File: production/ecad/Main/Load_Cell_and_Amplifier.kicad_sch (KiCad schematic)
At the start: 19 parts, among them Q3 MMBT4403, U3 HX711

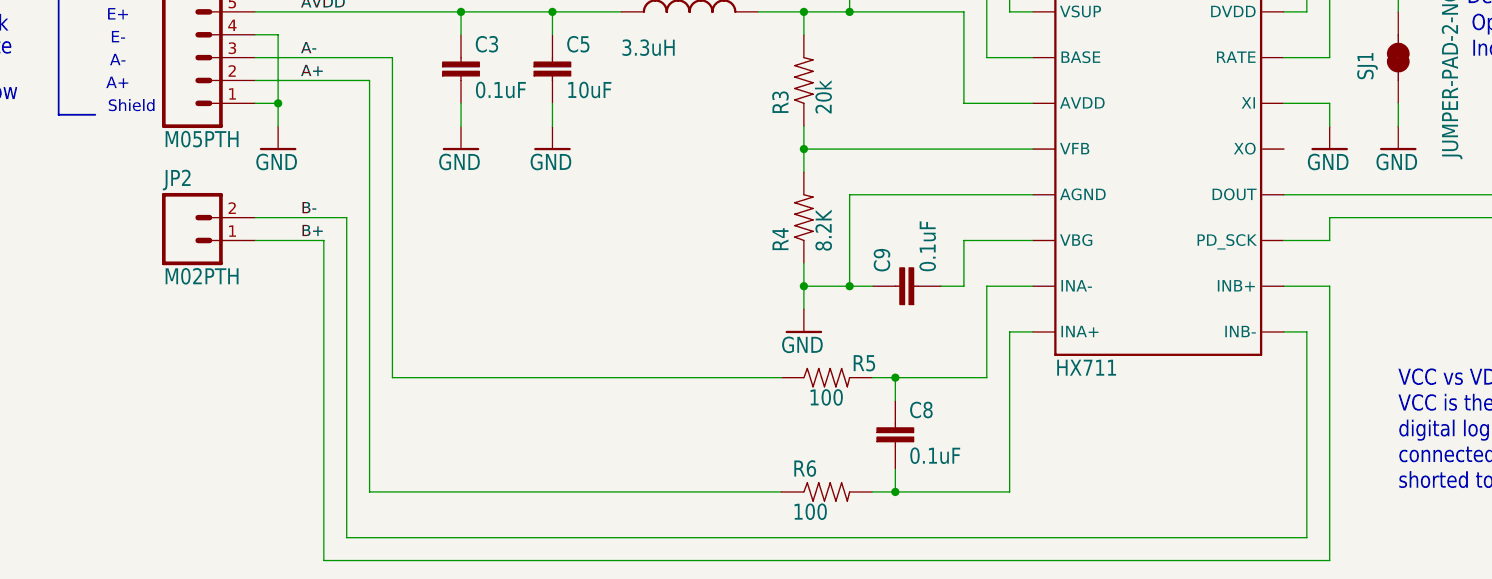
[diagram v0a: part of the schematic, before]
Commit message: deleted B pins bc we won use them
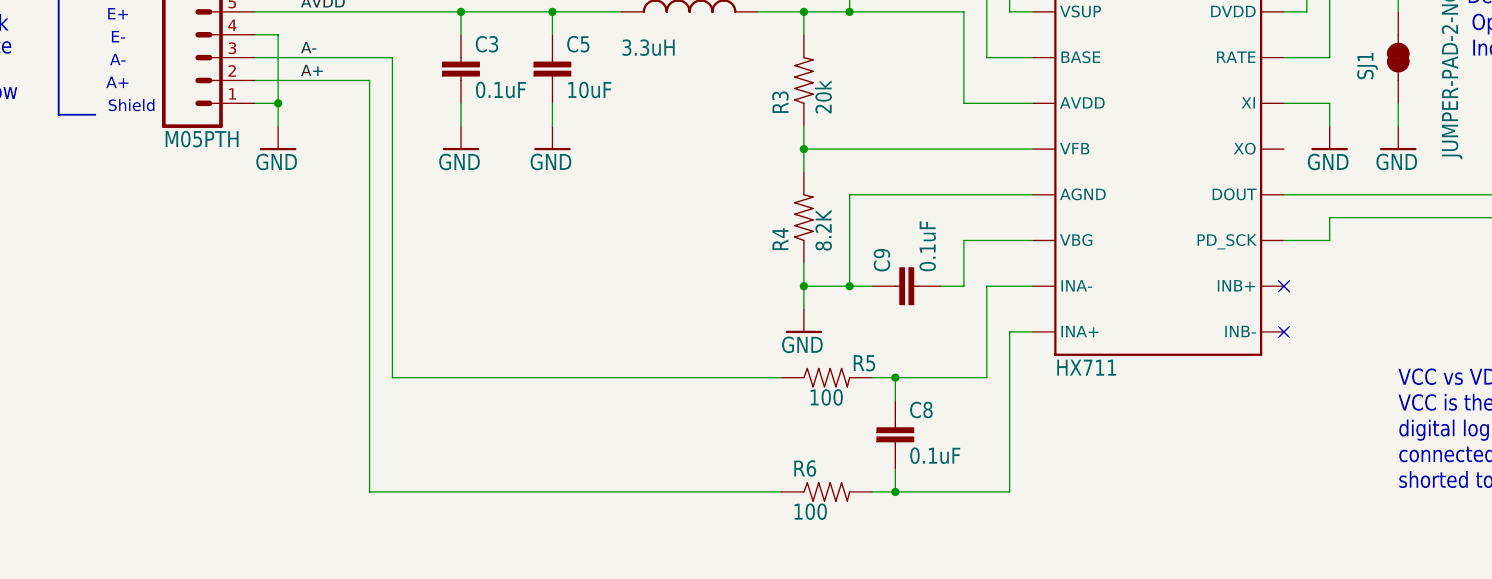
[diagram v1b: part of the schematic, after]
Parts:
- removed JP2: M02PTH, Load Cell and Amplifier:1X02, symbol Load Cell and Amplifier-eagle-import:M02PTH
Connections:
- net B+: no longer names the net of U3.10 (INB+)
- net B-: no longer names the net of U3.9 (INB-)
- no-connect marks 0 -> 2
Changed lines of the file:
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@@
 		(color 0 0 0 0)
 	)
+	(no_connect
+		(at 190.5 106.68)
+	)
+	(no_connect
+		(at 190.5 101.6)
+	)
 	(wire
 		(pts
@@
 	(wire
 		(pts
-			(xy 190.5 106.68) (xy 193.04 106.68)
-		)
-		(stroke
-			(width 0.1524)
-			(type solid)
-		)
-	)
-	(wire
-		(pts
 			(xy 190.5 81.28) (xy 195.58 81.28)
 		)
@@
 	(wire
 		(pts
-			(xy 83.82 96.52) (xy 76.2 96.52)
-		)
-		(stroke
-			(width 0.1524)
-			(type solid)
-		)
-	)
-	(wire
-		(pts
 			(xy 144.78 101.6) (xy 142.24 101.6)
 		)
@@
 	(wire
 		(pts
-			(xy 193.04 106.68) (xy 193.04 129.54)
-		)
-		(stroke
-			(width 0.1524)
-			(type solid)
-		)
-	)
-	(wire
-		(pts
 			(xy 101.6 55.88) (xy 101.6 53.34)
 		)
@@
 		(pts
 			(xy 203.2 68.58) (xy 203.2 71.12)
-		)
-		(stroke
-			(width 0.1524)
-			(type solid)
-		)
-	)
-	(wire
-		(pts
-			(xy 83.82 132.08) (xy 83.82 96.52)
 		)
 		(stroke
@@
 	(wire
 		(pts
-			(xy 86.36 129.54) (xy 86.36 93.98)
-		)
-		(stroke
-			(width 0.1524)
-			(type solid)
-		)
-	)
-	(wire
-		(pts
 			(xy 129.54 45.72) (xy 129.54 43.18)
-		)
-		(stroke
-			(width 0.1524)
-			(type solid)
-		)
-	)
-	(wire
-		(pts
-			(xy 86.36 93.98) (xy 76.2 93.98)
 		)
 		(stroke
@@
 	(wire
 		(pts
-			(xy 195.58 132.08) (xy 83.82 132.08)
-		)
-		(stroke
-			(width 0.1524)
-			(type solid)
-		)
-	)
-	(wire
-		(pts
 			(xy 137.16 104.14) (xy 137.16 101.6)
 		)
@@
 		(pts
 			(xy 220.98 96.52) (xy 220.98 99.06)
-		)
-		(stroke
-			(width 0.1524)
-			(type solid)
-		)
-	)
-	(wire
-		(pts
-			(xy 190.5 101.6) (xy 195.58 101.6)
 		)
 		(stroke
@@
 	(wire
 		(pts
-			(xy 193.04 129.54) (xy 86.36 129.54)
-		)
-		(stroke
-			(width 0.1524)
-			(type solid)
-		)
-	)
-	(wire
-		(pts
 			(xy 223.52 96.52) (xy 220.98 96.52)
 		)
@@
 		(pts
 			(xy 203.2 81.28) (xy 203.2 83.82)
-		)
-		(stroke
-			(width 0.1524)
-			(type solid)
-		)
-	)
-	(wire
-		(pts
-			(xy 195.58 101.6) (xy 195.58 132.08)
 		)
 		(stroke
@@
 	(label "AVDD"
 		(at 81.28 71.12 0)
-		(fields_autoplaced yes)
-		(effects
-			(font
-				(size 1.2446 1.2446)
-			)
-			(justify left bottom)
-		)
-	)
-	(label "B+"
-		(at 81.28 96.52 0)
-		(fields_autoplaced yes)
-		(effects
-			(font
-				(size 1.2446 1.2446)
-			)
-			(justify left bottom)
-		)
-	)
-	(label "B-"
-		(at 81.28 93.98 0)
 		(fields_autoplaced yes)
 		(effects
@@
 					(unit 1)
 				)
-			)
-		)
-	)
-	(symbol
-		(lib_id "Load Cell and Amplifier-eagle-import:M02PTH")
-		(at 68.58 96.52 0)
-		(unit 1)
-		(exclude_from_sim no)
-		(in_bom yes)
-		(on_board yes)
-		(dnp no)
-		(property "Reference" "JP2"
-			(at 66.04 90.678 0)
-			(effects
-				(font
-					(size 1.778 1.5113)
-				)
-				(justify left bottom)
-			)
-		)
-		(property "Value" "M02PTH"
-			(at 66.04 101.6 0)
-			(effects
-				(font
-					(size 1.778 1.5113)
-				)
-				(justify left bottom)
-			)
-		)
-		(property "Footprint" "Load Cell and Amplifier:1X02"
-			(at 68.58 96.52 0)
-			(effects
-				(font
-					(size 1.27 1.27)
-				)
-				(hide yes)
-			)
-		)
-		(property "Datasheet" ""
-			(at 68.58 96.52 0)
-			(effects
-				(font
-					(size 1.27 1.27)
-				)
-				(hide yes)
-			)
-		)
-		(property "Description" ""
-			(at 68.58 96.52 0)
-			(effects
-				(font
-					(size 1.27 1.27)
-				)
-				(hide yes)
-			)
-		)
-		(pin "1"
-		)
-		(pin "2"
-		)
-		(instances
-			(project "Main"
-				(path "/a34d77bc-8f6a-417e-a206-3165e6c5c658/1fa8e4ec-3b8f-41b7-8956-25ba2b294586"
-					(reference "JP2")
-					(unit 1)
-				)

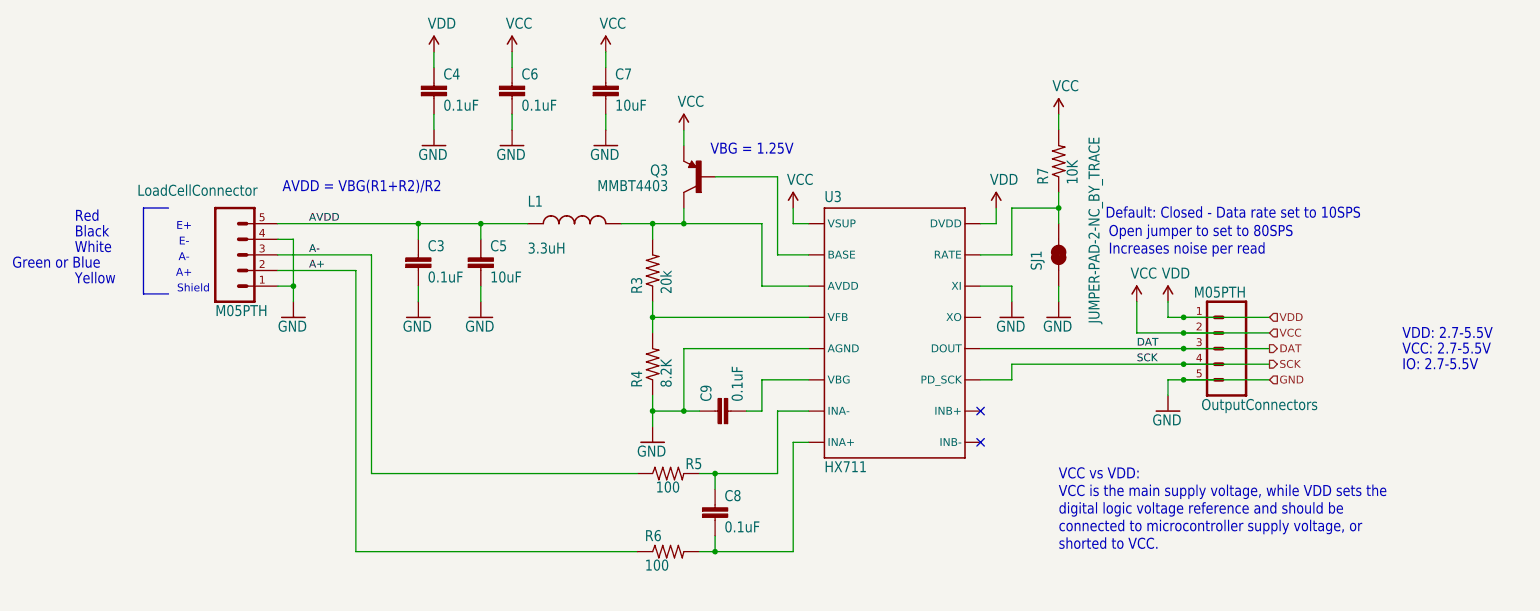
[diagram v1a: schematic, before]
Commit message: Added new load cell connector, erased old thru hole connector from data side because we just have it on the pcb
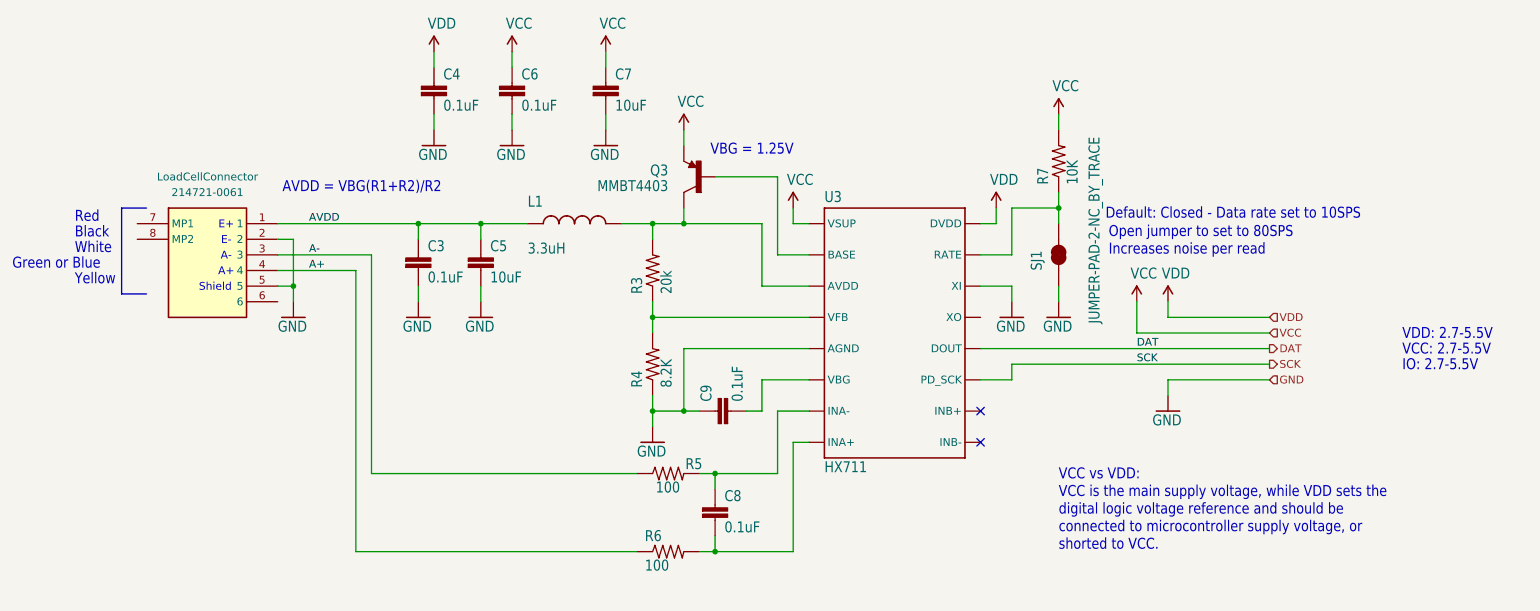
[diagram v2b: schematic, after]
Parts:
- removed LoadCellConnector, OutputConnectors: M05PTH, Load Cell and Amplifier:1X05, symbol Load Cell and Amplifier-eagle-import:M05PTH
- added LoadCellConnector: 214721-0061, 2147210061, symbol 6_pos_connector:214721-0061
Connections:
- net A+: now also LoadCellConnector.4
- net A-: now also LoadCellConnector.3
- net AVDD: now also LoadCellConnector.1
- net GND: now also LoadCellConnector.2, LoadCellConnector.5
